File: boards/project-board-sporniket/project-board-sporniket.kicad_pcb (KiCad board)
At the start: 2 copper layers, 100 x 110 mm, 40 parts, among them J1 ⊕, J101 a, J102 b, J103 c, J104 d, J105 e, J106 f, J107 g, J108 h, J109 i, J110 j, J111 k, J112 l, J113 m, J114 n, J115 o, J116 p, J117 q, J118 r, J119 s, J120 t, J121 u, J122 v, J123 w, J124 x, J2 ⊕, J3 ⊕, J4 ⊕, J5 ⊖, J6 ⊖, J7 ⊖, J8 ⊖

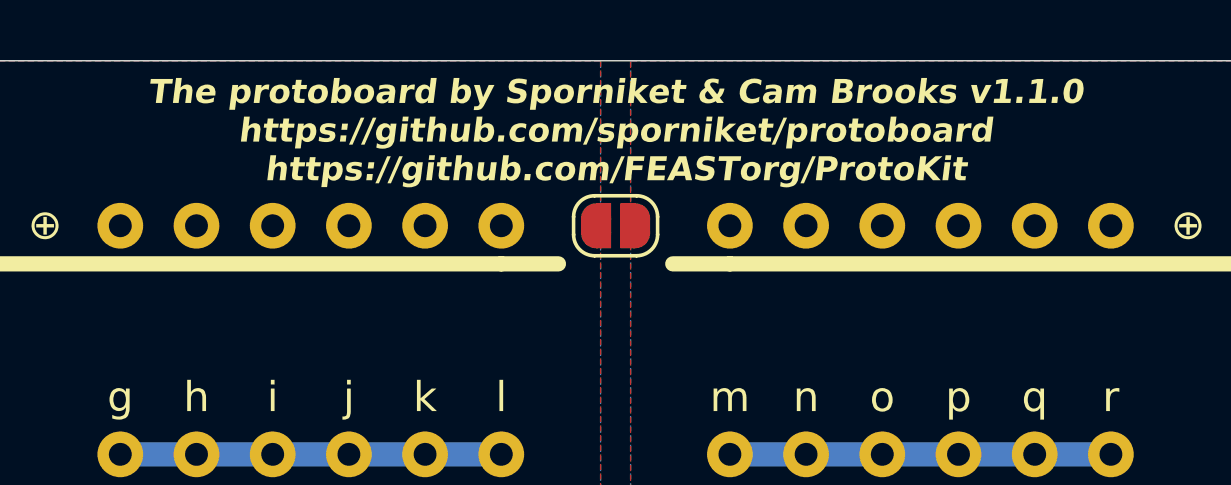
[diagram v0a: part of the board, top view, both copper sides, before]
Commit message: refactor: org casing rename from 'FEASTorg' to 'feastorg'
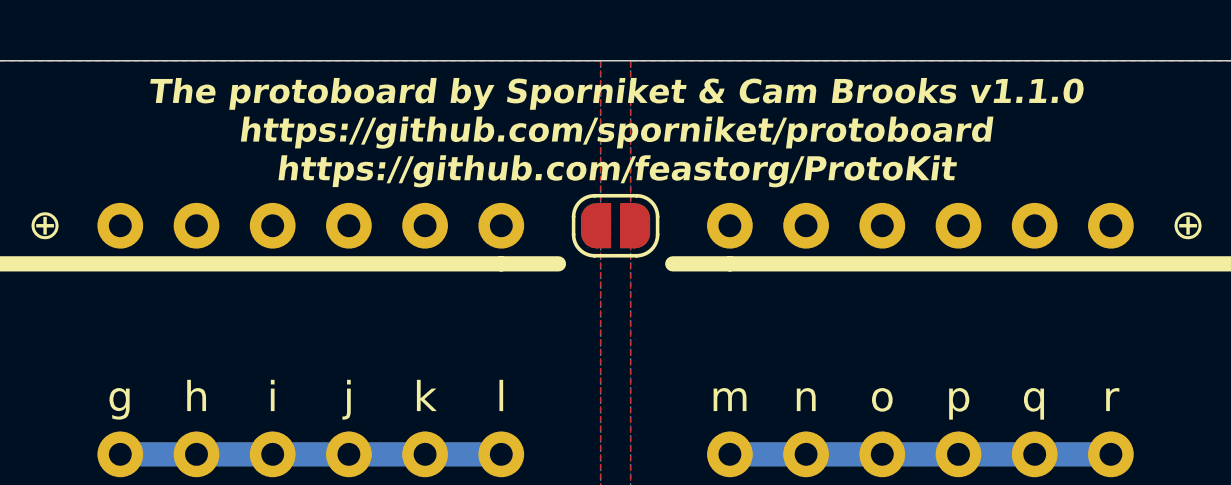
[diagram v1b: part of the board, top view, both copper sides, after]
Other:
- board text added: "The protoboard by Sporniket & Cam Brooks v1.1.0 https://github.com/sporniket/protoboard https://github.com/feastorg/ProtoKit"
- board text removed: "The protoboard by Sporniket & Cam Brooks v1.1.0 https://github.com/sporniket/protoboard https://github.com/FEASTorg/ProtoKit"
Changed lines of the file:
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@@
 		)
 	)
-	(gr_text "The protoboard by Sporniket & Cam Brooks v1.1.0\nhttps://github.com/sporniket/protoboard\nhttps://github.com/FEASTorg/ProtoKit"
+	(gr_text "The protoboard by Sporniket & Cam Brooks v1.1.0\nhttps://github.com/sporniket/protoboard\nhttps://github.com/feastorg/ProtoKit"
 		(at 100.11 92.385 0)
 		(layer "F.SilkS")
